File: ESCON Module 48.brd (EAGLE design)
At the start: 167.6 x 101.6 mm, 76 parts, among them U1 ESDA14V2SC6, U2 ESDA14V2SC6, U3 ESDA14V2SC6, X1 TERMINAL-BLOCK-3.5MM-2-PIN-LO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, X11 JST-XH-02-PIN-LONG-PAD, X12 JST-XH-03-PIN-LONG-PAD, X13 JST-XH-04-PIN-LONG-PAD, X14 JST-XH-03-PIN-LONG-PAD, X15 JST-XH-05-PIN-LONG-PAD, X17 JST-XH-02-PIN-LONG-PAD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

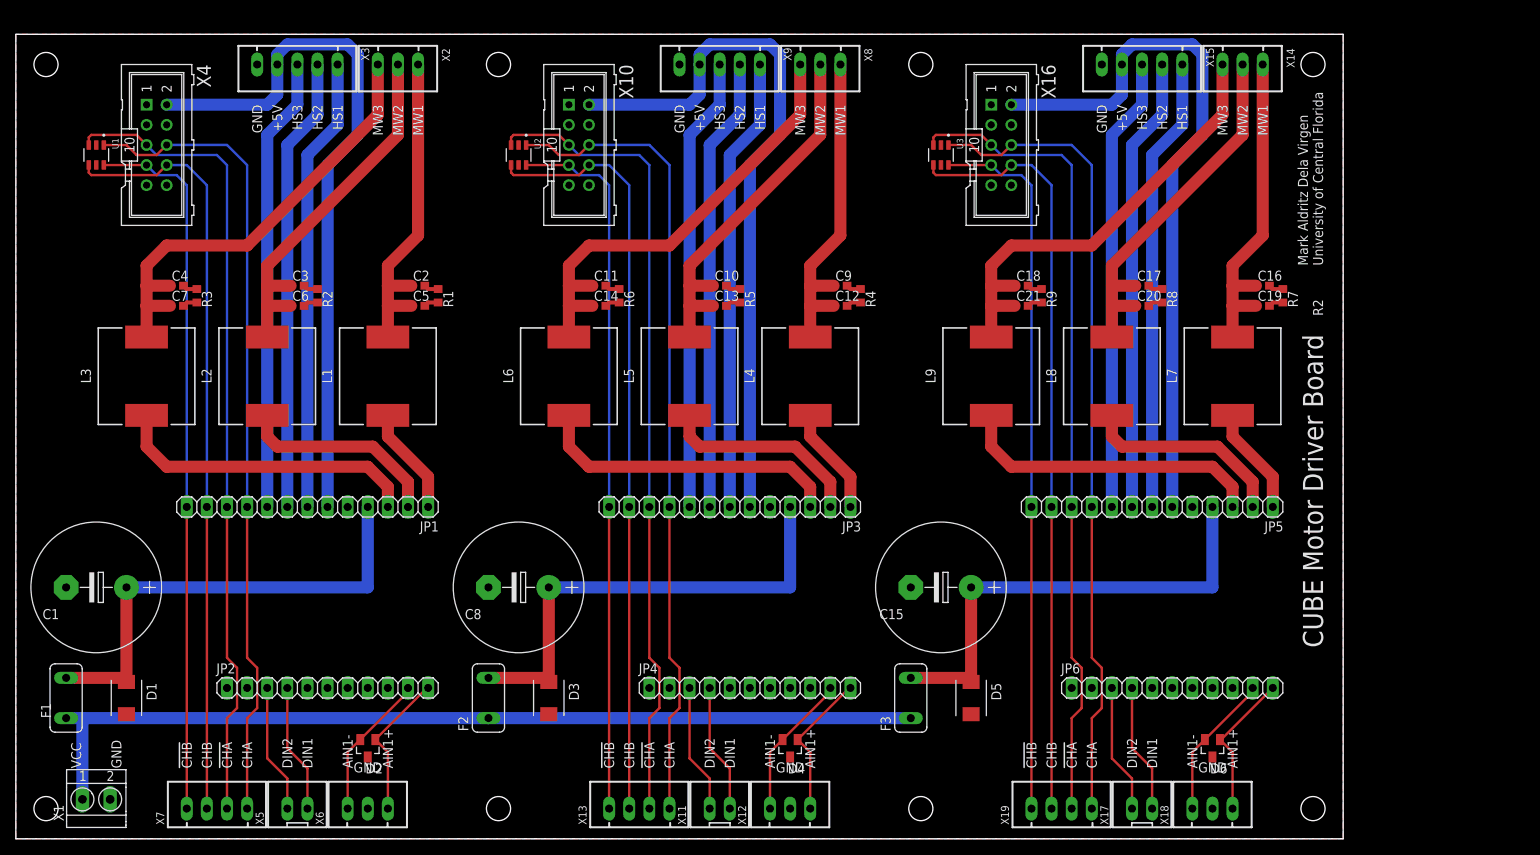
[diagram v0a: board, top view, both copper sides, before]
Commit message: Bigger capacitors
Added support for 3300uF capacitors
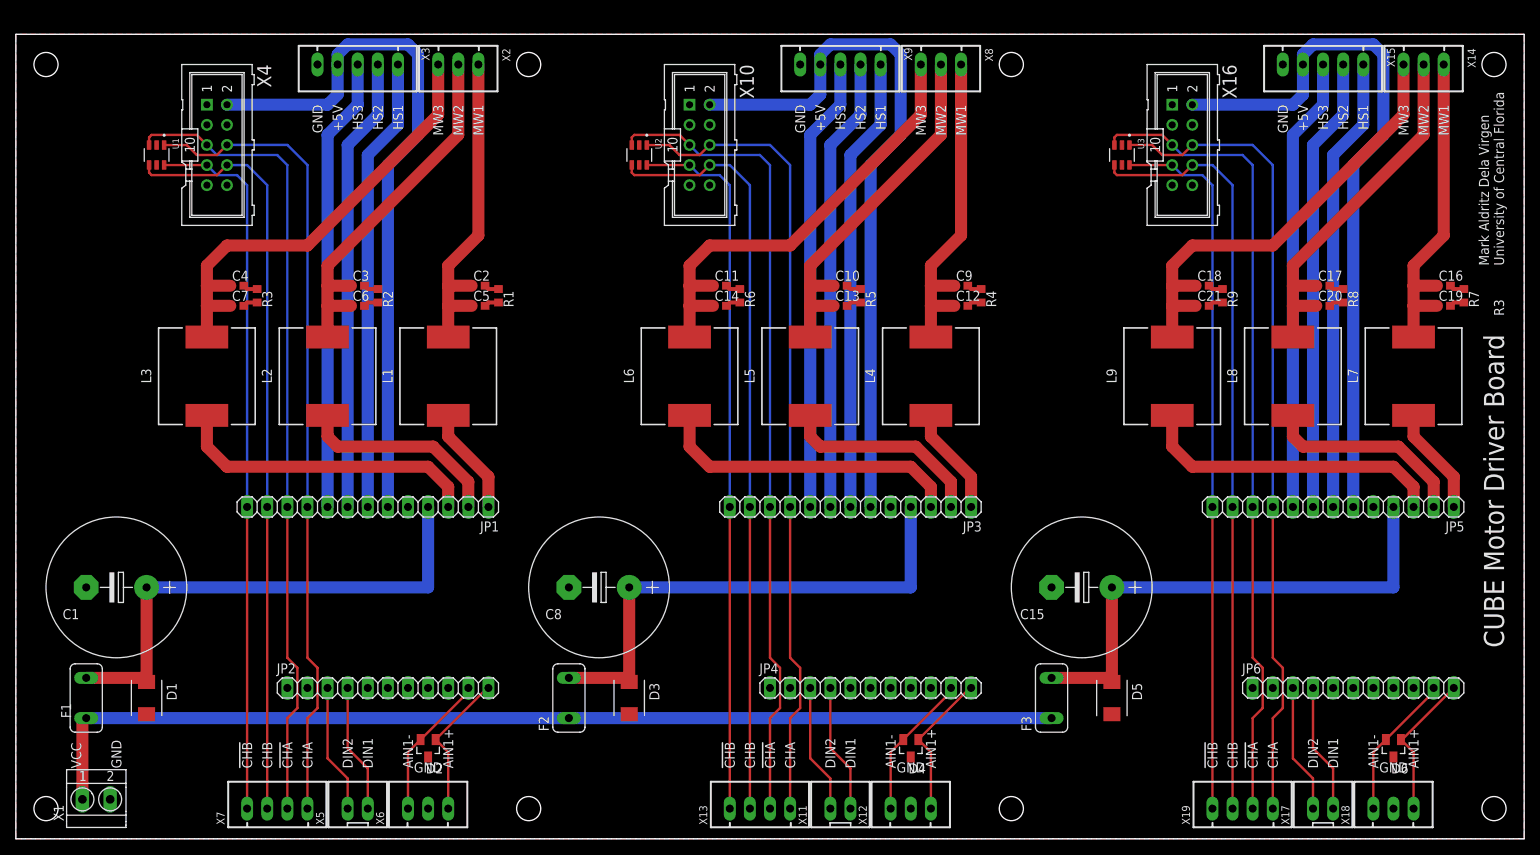
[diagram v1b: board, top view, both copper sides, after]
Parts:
- C1, C15, C8: value 120uF -> 3300uF; device rcl:E7,5-16 -> rcl:E7,5-18
- moved C16 22.9 mm to (180.3, 69.8)
- moved C18 22.9 mm to (149.9, 69.8)
- moved C19 22.9 mm to (180.3, 67.3)
- moved C21 22.9 mm to (149.9, 67.3)
- moved D6 22.9 mm to (174.0, 11.4)
- moved JP5 22.9 mm to (166.4, 41.9)
- moved L7 22.9 mm to (176.5, 58.4)
- moved L9 22.9 mm to (146.1, 58.4)
- moved R9 22.9 mm to (152.4, 68.6)
- moved X14 22.9 mm to (177.8, 97.8)
- moved X18 22.9 mm to (174.0, 3.81)
- moved X16 22.9 mm to (147.3, 87.6)
- moved C17 22.9 mm to (165.1, 69.8)
- moved C20 22.9 mm to (165.1, 67.3)
- moved JP6 22.9 mm to (168.9, 19.1)
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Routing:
- net VCC: track 116.9 -> 132.7 mm
- net VDD_C: track 60.7 -> 65.8 mm
- net VDD_B: track 60.2 -> 65.3 mm
- net VDD_A: track 60.2 -> 65.3 mm
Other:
- board size 167.6 x 101.6 mm -> 190.5 x 101.6 mm
- board text added: "R3"
- board text removed: "R2"
